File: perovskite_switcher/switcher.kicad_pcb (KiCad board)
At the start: 2 copper layers, 45 parts, among them J1 G125-MV12605M1P, Q1 DMC2053UVT, U1 SN74LVC1G14DRL, U10 MAX4736EUBT, U11 MAX4736EUBT, U12 MAX4736EUBT, U13 MAX4736EUBT, U14 MAX4736EUBT, U15 LT3092ETS8TRPBF, U16 INA180B2IDBVT, U17 MCP6401RT-xOT, U2 CD4518BM96, U3 CD4028BMT, U4 CD4028BMT, U5 MAX4736EUBT, U6 MAX4736EUBT, U7 MAX4736EUBT, U8 MAX4736EUBT, U9 MAX4736EUBT

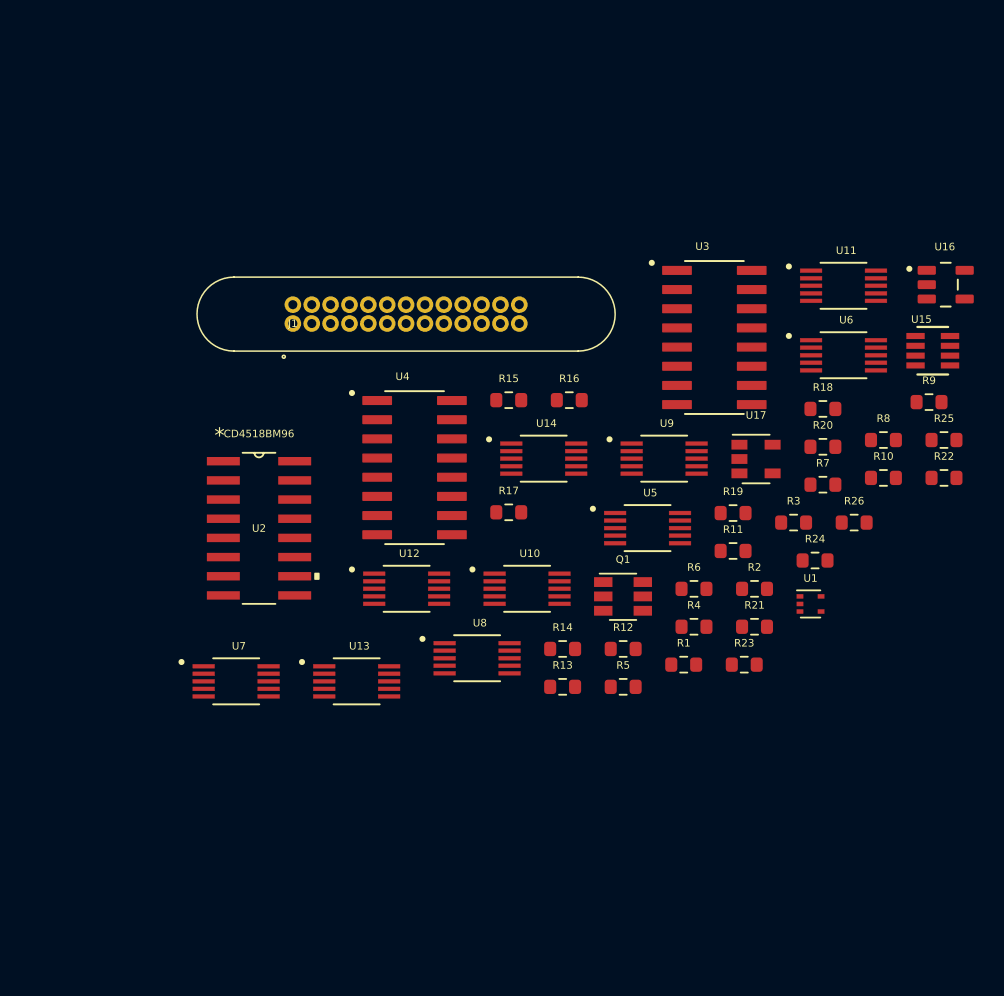
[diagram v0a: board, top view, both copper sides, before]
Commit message: Update boards
- Added flight computer board outline
- Added GUI for curve tracer
- Updated curve tracer
- Updated perovskite switcher
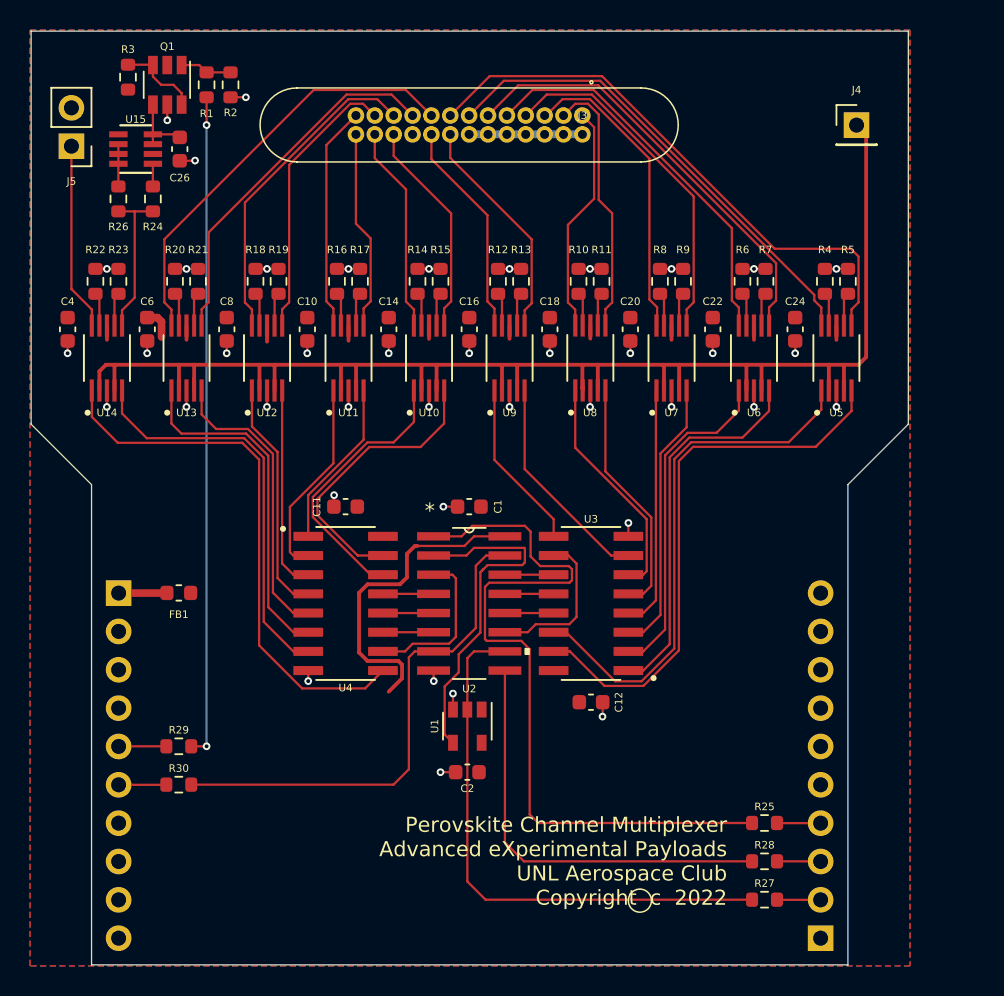
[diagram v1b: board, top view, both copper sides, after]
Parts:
- removed U16: INA180B2IDBVT, INA180B2IDBVT:SOT95P280X145-5N
- removed U17: MCP6401RT-xOT, Package_TO_SOT_SMD:SOT-23-5
- added C1: 0.1u, Capacitor_SMD:C_0603_1608Metric, F.Cu at (153.9, 100.3)
- added C10: 0.1u, Capacitor_SMD:C_0603_1608Metric, F.Cu at (143.1, 88.6)
- added C11: 0.1u, Capacitor_SMD:C_0603_1608Metric, F.Cu at (145.7, 100.3)
- added C12: 0.1u, Capacitor_SMD:C_0603_1608Metric, F.Cu at (161.9, 113.3)
- added C14: 0.1u, Capacitor_SMD:C_0603_1608Metric, F.Cu at (148.5, 88.6)
- added C16: 0.1u, Capacitor_SMD:C_0603_1608Metric, F.Cu at (153.9, 88.6)
- added C18: 0.1u, Capacitor_SMD:C_0603_1608Metric, F.Cu at (159.2, 88.6)
- added C2: 0.1u, Capacitor_SMD:C_0603_1608Metric, F.Cu at (153.7, 117.9)
- added C20: 0.1u, Capacitor_SMD:C_0603_1608Metric, F.Cu at (164.5, 88.6)
- added C22: 0.1u, Capacitor_SMD:C_0603_1608Metric, F.Cu at (170.0, 88.6)
- added C24: 0.1u, Capacitor_SMD:C_0603_1608Metric, F.Cu at (175.5, 88.6)
- added C26: 0.1u, Capacitor_SMD:C_0603_1608Metric, F.Cu at (134.7, 76.6)
- added C4: 0.1u, Capacitor_SMD:C_0603_1608Metric, F.Cu at (127.3, 88.6)
- added C6: 0.1u, Capacitor_SMD:C_0603_1608Metric, F.Cu at (132.5, 88.6)
- added C8: 0.1u, Capacitor_SMD:C_0603_1608Metric, F.Cu at (137.8, 88.6)
- added FB1: Ferrite_Bead, Inductor_SMD:L_0603_1608Metric, F.Cu at (134.6, 106.0)
- added J2: Conn_01x10_Female, Connector_PinHeader_2.54mm:PinHeader_1x10_P2.54mm_Vertical, B.Cu at (177.1, 128.9)
- added J3: G125-MV12605M1P, LIB_G125-MV12605M1P:G125-MV12605M1P, F.Cu at (161.4, 74.4)
- added J4: Panel Output to Curve Tracer, Connector_PinHeader_2.54mm:PinHeader_1x01_P2.54mm_Vertical, F.Cu at (179.5, 75.1)
- added J5: Silicon Cell, Connector_PinHeader_2.54mm:PinHeader_1x02_P2.54mm_Vertical, F.Cu at (127.5, 76.5)
- added R27: 100, Resistor_SMD:R_0603_1608Metric, F.Cu at (173.4, 126.4)
- added R28: 100, Resistor_SMD:R_0603_1608Metric, F.Cu at (173.4, 123.8)
- added R29: 100, Resistor_SMD:R_0603_1608Metric, F.Cu at (134.6, 116.2)
- added R30: 100, Resistor_SMD:R_0603_1608Metric, F.Cu at (134.6, 118.7)
- J1: value G125-MV12605M1P -> Conn_01x10_Female; footprint LIB_G125-MV12605M1P:G125-MV12605M1P -> Connector_PinHeader_2.54mm:PinHeader_1x10_P2.54mm_Vertical; moved to B.Cu
- R25: value R -> 100
- U1: footprint Package_TO_SOT_SMD:SOT-553 -> Package_TO_SOT_SMD:SOT-23-5
- moved R22 57.7 mm to (129.1, 85.4), turned to 270 degrees
- moved U15 54.5 mm to (131.8, 76.6)
- moved R26 53.2 mm to (130.6, 79.9), turned to 90 degrees
- moved R3 53.1 mm to (131.3, 71.9), turned to 90 degrees
- moved R24 50.0 mm to (132.9, 79.9), turned to 90 degrees
- moved R1 49.7 mm to (136.5, 72.4), turned to 270 degrees
- moved R23 48.6 mm to (130.6, 85.4), turned to 270 degrees
- moved R2 48.2 mm to (138.0, 72.4), turned to 270 degrees
- moved Q1 45.4 mm to (133.9, 72.4), turned to 270 degrees
- moved R20 44.3 mm to (134.4, 85.4), turned to 270 degrees
- moved R21 43.4 mm to (135.9, 85.4), turned to 270 degrees
- moved R18 38.5 mm to (139.7, 85.4), turned to 270 degrees
- moved U7 35.9 mm to (167.3, 90.5), turned to 90 degrees
- moved R19 33.8 mm to (141.2, 85.4), turned to 270 degrees
- moved U11 33.1 mm to (145.9, 90.5), turned to 90 degrees
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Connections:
- net /Perovskite Switches/ENABLE_PANEL_SWITCH renamed ENABLE_PANEL_SWITCH
- net /Perovskite Switches/RESET_PANEL_SWITCH renamed RESET_PANEL_SWITCH
- J1 pad 1: Net-(J1-Pad1) -> Net-(FB1-Pad2)
- R1 pad 2: /Perovskite Switches/ENABLE_TEST_SOURCE -> ENABLE_TEST_SOURCE
- R25 pad 1: /Perovskite Switches/V_PANEL -> 0-9_CLOCK
- R25 pad 2: Net-(R25-Pad2) -> Net-(J2-Pad4)
- U10 pad 10: Net-(J1-Pad11) -> Net-(J3-Pad25)
- U10 pad 2: Net-(R25-Pad2) -> Net-(J4-Pad1)
- U10 pad 4: Net-(R25-Pad2) -> Net-(J4-Pad1)
- U10 pad 6: Net-(J1-Pad12) -> Net-(J3-Pad24)
- U11 pad 10: Net-(J1-Pad13) -> Net-(J3-Pad13)
- U11 pad 2: Net-(R25-Pad2) -> Net-(J4-Pad1)
- U11 pad 4: Net-(R25-Pad2) -> Net-(J4-Pad1)
- U11 pad 6: Net-(J1-Pad19) -> Net-(J3-Pad26)
- U12 pad 10: Net-(J1-Pad18) -> Net-(J3-Pad11)
- U12 pad 2: Net-(R25-Pad2) -> Net-(J4-Pad1)
- U12 pad 4: Net-(R25-Pad2) -> Net-(J4-Pad1)
- U12 pad 6: Net-(J1-Pad17) -> Net-(J3-Pad12)
- U13 pad 10: Net-(J1-Pad16) -> Net-(J3-Pad9)
- U13 pad 2: Net-(R25-Pad2) -> Net-(J4-Pad1)
- U13 pad 4: Net-(R25-Pad2) -> Net-(J4-Pad1)
- U13 pad 6: Net-(J1-Pad15) -> Net-(J3-Pad10)
- U14 pad 10: Net-(J1-Pad14) -> Net-(J5-Pad1)
- U14 pad 2: Net-(R25-Pad2) -> Net-(J4-Pad1)
- U14 pad 4: Net-(R25-Pad2) -> Net-(J4-Pad1)
- U2 pad 1: /Perovskite Switches/0-9_CLOCK -> 0-9_CLOCK
- U2 pad 9: /Perovskite Switches/10-19_CLOCK -> 10-19_CLOCK
- U3 pad 10: Net-(U2-Pad3) -> Net-(U2-Pad11)
- U3 pad 11: Net-(U2-Pad6) -> Net-(U2-Pad14)
- U3 pad 12: Net-(U2-Pad5) -> Net-(U2-Pad13)
- U3 pad 13: Net-(U2-Pad4) -> Net-(U2-Pad12)
- U4 pad 1: Net-(U12-Pad5) -> Net-(U11-Pad5)
- U4 pad 10: Net-(U2-Pad11) -> Net-(U2-Pad3)
- U4 pad 11: Net-(U2-Pad14) -> Net-(U2-Pad6)
- U4 pad 12: Net-(U2-Pad13) -> Net-(U2-Pad5)
- U4 pad 13: Net-(U2-Pad12) -> Net-(U2-Pad4)
- U4 pad 15: Net-(U11-Pad1) -> Net-(U10-Pad5)
- U4 pad 2: Net-(U11-Pad5) -> Net-(U11-Pad1)
- U4 pad 3: Net-(U10-Pad5) -> Net-(U12-Pad5)
- U4 pad 4: Net-(U13-Pad1) -> Net-(U12-Pad1)
- U4 pad 5: Net-(U14-Pad1) -> Net-(U13-Pad5)
- U4 pad 6: Net-(U12-Pad1) -> Net-(U13-Pad1)
- U4 pad 7: Net-(U13-Pad5) -> Net-(U14-Pad5)
- U4 pad 9: Net-(U14-Pad5) -> Net-(U14-Pad1)
- U5 pad 10: Net-(J1-Pad1) -> Net-(J3-Pad7)
- U5 pad 2: Net-(R25-Pad2) -> Net-(J4-Pad1)
- U5 pad 4: Net-(R25-Pad2) -> Net-(J4-Pad1)
- U5 pad 5: Net-(U3-Pad3) -> Net-(U3-Pad15)
- U5 pad 6: Net-(J1-Pad2) -> Net-(J3-Pad8)
- U6 pad 1: Net-(U3-Pad15) -> Net-(U3-Pad2)
- U6 pad 10: Net-(J1-Pad3) -> Net-(J3-Pad5)
- U6 pad 2: Net-(R25-Pad2) -> Net-(J4-Pad1)
- U6 pad 4: Net-(R25-Pad2) -> Net-(J4-Pad1)
- U6 pad 5: Net-(U3-Pad2) -> Net-(U3-Pad1)
- U6 pad 6: Net-(J1-Pad4) -> Net-(J3-Pad6)
- U7 pad 1: Net-(U3-Pad6) -> Net-(U3-Pad4)
- U7 pad 10: Net-(J1-Pad5) -> Net-(J3-Pad3)
- U7 pad 2: Net-(R25-Pad2) -> Net-(J4-Pad1)
- U7 pad 4: Net-(R25-Pad2) -> Net-(J4-Pad1)
- U7 pad 5: Net-(U3-Pad1) -> Net-(U3-Pad3)
- U7 pad 6: Net-(J1-Pad6) -> Net-(J3-Pad4)
- U8 pad 1: Net-(U3-Pad4) -> Net-(U3-Pad6)
- U8 pad 10: Net-(J1-Pad7) -> Net-(J3-Pad1)
- U8 pad 2: Net-(R25-Pad2) -> Net-(J4-Pad1)
- U8 pad 4: Net-(R25-Pad2) -> Net-(J4-Pad1)
- U8 pad 5: Net-(U3-Pad7) -> Net-(U3-Pad5)
- U8 pad 6: Net-(J1-Pad8) -> Net-(J3-Pad2)
- U9 pad 1: Net-(U3-Pad5) -> Net-(U3-Pad9)
- U9 pad 10: Net-(J1-Pad9) -> Net-(J3-Pad22)
- U9 pad 2: Net-(R25-Pad2) -> Net-(J4-Pad1)
- U9 pad 4: Net-(R25-Pad2) -> Net-(J4-Pad1)
- U9 pad 5: Net-(U3-Pad9) -> Net-(U3-Pad7)
- U9 pad 6: Net-(J1-Pad10) -> Net-(J3-Pad21)
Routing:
- net Net-(J4-Pad1): track 0.00 -> 100.7 mm
- net GND: track 0.00 -> 51.9 mm, vias 0 -> 41
- net 0-9_CLOCK: track 0.00 -> 50.9 mm
- net ENABLE_TEST_SOURCE: track 0.00 -> 44.0 mm, vias 0 -> 2
- net Net-(J3-Pad8): track 0.00 -> 37.8 mm
- net Net-(U3-Pad15): track 0.00 -> 36.9 mm
- net ENABLE_PANEL_SWITCH: track 0.00 -> 36.8 mm
- net Net-(U14-Pad1): track 0.00 -> 36.2 mm
- net Net-(U3-Pad14): track 0.00 -> 35.1 mm
- net RESET_PANEL_SWITCH: track 0.00 -> 33.8 mm
- net +3V3: track 0.00 -> 33.1 mm
- net Net-(J3-Pad7): track 0.00 -> 31.9 mm
- net Net-(J3-Pad6): track 0.00 -> 29.1 mm
- net Net-(J3-Pad9): track 0.00 -> 28.4 mm
- net 10-19_CLOCK: track 0.00 -> 28.3 mm
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- added copper zone on F.Cu, net +3V3
- added copper zone on B.Cu, net GND
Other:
- board outline added: 58.1 x 61.8 mm
- net class Default: clearance 0.2 -> 0.1524; trace_width 0.25 -> 0.1524; via_dia 0.8 -> 0.508; via_drill 0.4 -> 0.254
- rule trace_clearance: 0.2 -> 0.1524
- rule trace_min: 0.2 -> 0.1524
- rule via_min_drill: 0.3 -> 0.254
- rule via_min_size: 0.4 -> 0.508
- board text added: "Perovskite Channel Multiplexer Advanced eXperimental Payloads UNL Aerospace Club Copyright c 2022"
